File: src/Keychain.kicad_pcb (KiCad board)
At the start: 2 copper layers, 50 x 75 mm, 21 parts, among them M1 Motor_DC, Q1 NPN, SW1 SW_Push

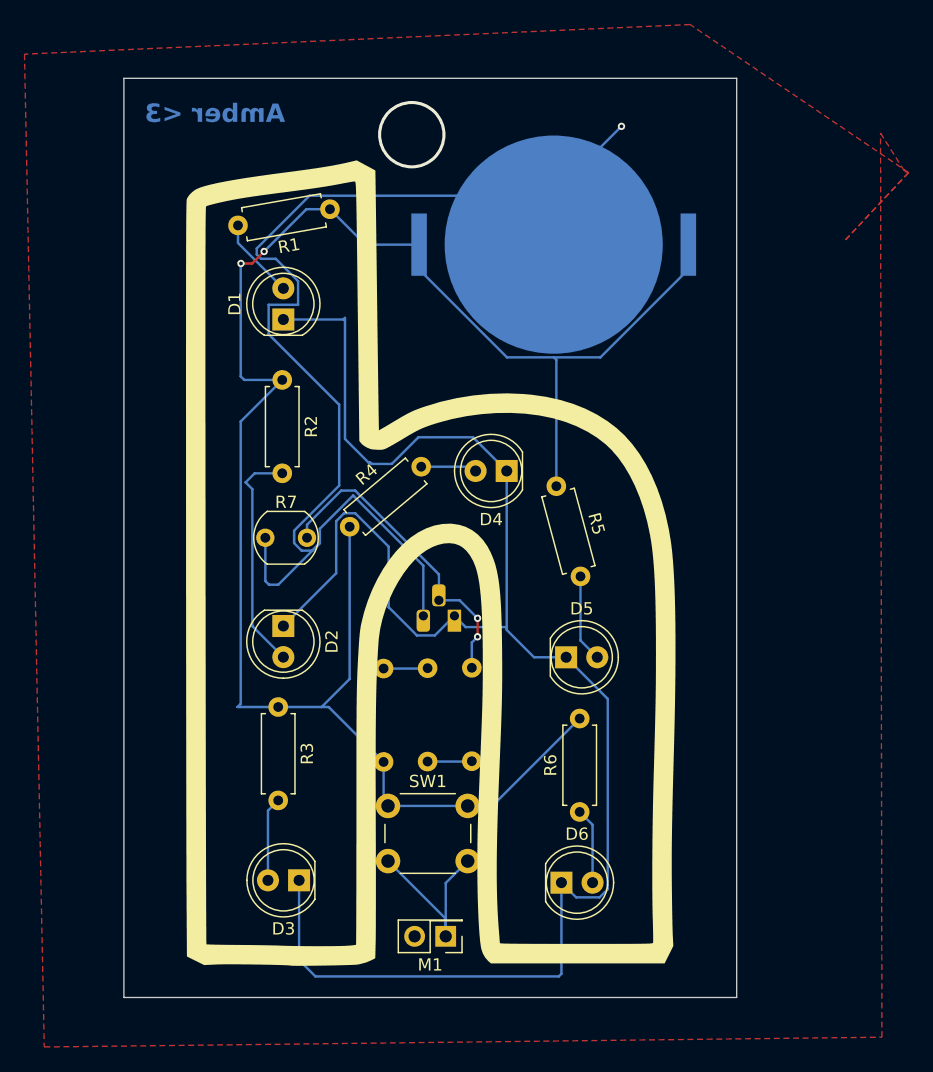
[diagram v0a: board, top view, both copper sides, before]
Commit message: rounded corners!
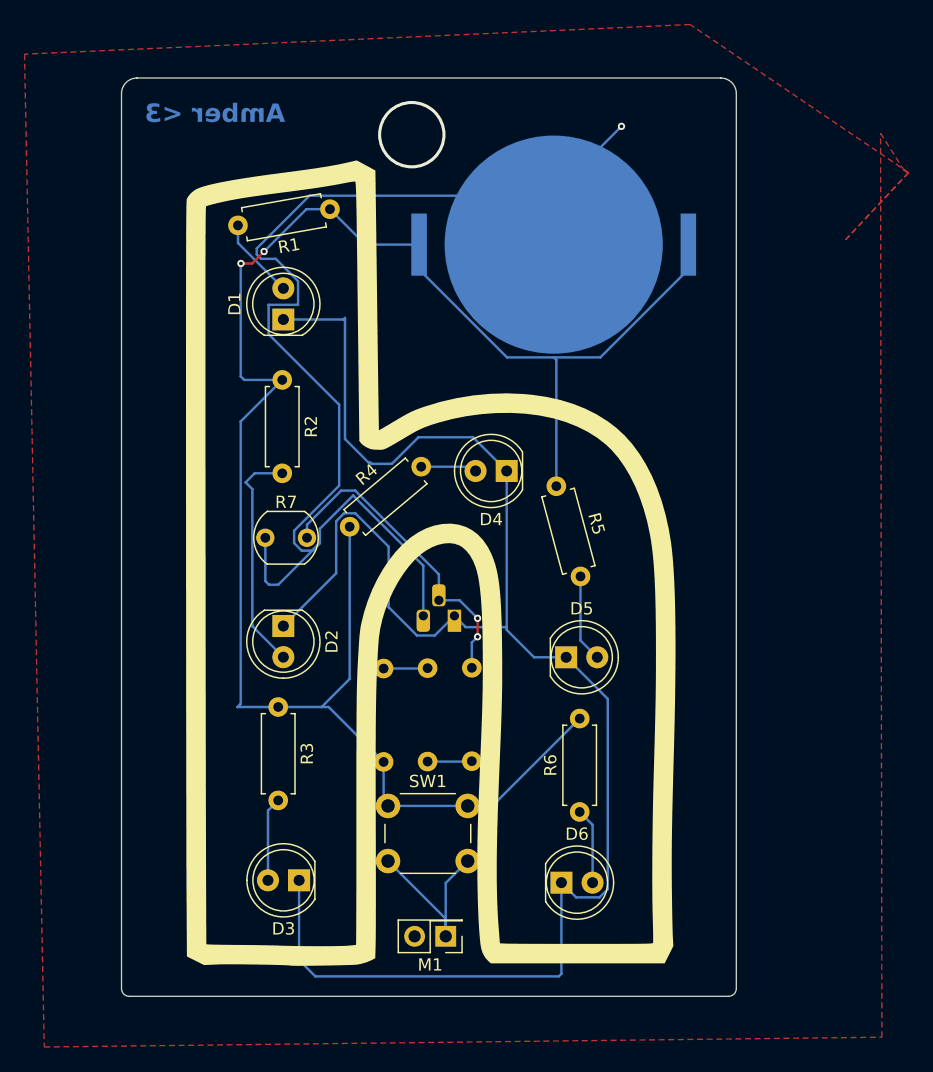
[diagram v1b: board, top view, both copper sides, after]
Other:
- board size 50 x 75 mm -> 50.2 x 74.9 mm
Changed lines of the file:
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@@
 		(tags "tact sw push 6mm")
 		(property "Reference" "SW1"
-			(at 3.25 -2 360)
+			(at 3.25 -2 0)
 			(layer "F.SilkS")
 			(effects
@@
 		)
 		(property "Value" "SW_Push"
-			(at 3.75 6.7 360)
+			(at 3.75 6.7 0)
 			(layer "F.Fab")
 			(effects
@@
 		)
 		(fp_text user "${REFERENCE}"
-			(at 3.25 2.25 360)
+			(at 3.25 2.25 0)
 			(layer "F.Fab")
 			(effects
@@
 		)
 		(fp_text user "${REFERENCE}"
-			(at 8.32 -4.371924 10)
+			(at 8.32 -4.371923 10)
 			(layer "F.Fab")
 			(effects
@@
 		(tags "Through hole pin header THT 2x01 2.54mm double row")
 		(property "Reference" "M1"
-			(at 1.27 -2.33 360)
+			(at 1.27 -2.33 0)
 			(layer "F.SilkS")
 			(effects
@@
 		)
 		(property "Value" "Motor_DC"
-			(at 1.27 2.33 360)
+			(at 1.27 2.33 0)
 			(layer "F.Fab")
 			(effects
@@
 		(tags "Resistor LDR5.1x3.4mm")
 		(property "Reference" "R7"
-			(at 1.7 -2.9 360)
+			(at 1.7 -2.9 0)
 			(layer "F.SilkS")
 			(effects
@@
 		)
 		(property "Value" "R_Photo"
-			(at 1.5 3 360)
+			(at 1.5 3 0)
 			(layer "F.Fab")
 			(effects
@@
 		)
 		(fp_text user "${REFERENCE}"
-			(at 1.7 -2.9 360)
+			(at 1.7 -2.9 0)
 			(layer "F.Fab")
 			(effects
@@
 		(tags "LED")
 		(property "Reference" "D4"
-			(at 1.27 -3.96 360)
+			(at 1.27 -3.96 0)
 			(layer "F.SilkS")
 			(effects
@@
 		)
 		(property "Value" "LED"
-			(at 1.27 3.96 360)
+			(at 1.27 3.96 0)
 			(layer "F.Fab")
 			(effects
@@
 		)
 		(property "Footprint" "LED_THT:LED_D5.0mm"
-			(at 0 0 360)
+			(at 0 0 0)
 			(layer "F.Fab")
 			(hide yes)
@@
 		)
 		(property "Datasheet" ""
-			(at 0 0 360)
+			(at 0 0 0)
 			(layer "F.Fab")
 			(hide yes)
@@
 		)
 		(property "Description" "Light emitting diode"
-			(at 0 0 360)
+			(at 0 0 0)
 			(layer "F.Fab")
 			(hide yes)
@@
 		)
 		(fp_text user "${REFERENCE}"
-			(at 1.27 0 360)
+			(at 1.27 0 0)
 			(layer "F.Fab")
 			(effects
@@
 		(tags "LED")
 		(property "Reference" "D3"
-			(at 1.27 -3.96 360)
+			(at 1.27 -3.96 0)
 			(layer "F.SilkS")
 			(effects
@@
 		)
 		(property "Value" "LED"
-			(at 1.27 3.96 360)
+			(at 1.27 3.96 0)
 			(layer "F.Fab")
 			(effects
@@
 		)
 		(property "Footprint" "LED_THT:LED_D5.0mm"
-			(at 0 0 360)
+			(at 0 0 0)
 			(layer "F.Fab")
 			(hide yes)
@@
 		)
 		(property "Datasheet" ""
-			(at 0 0 360)
+			(at 0 0 0)
 			(layer "F.Fab")
 			(hide yes)
@@
 		)
 		(property "Description" "Light emitting diode"
-			(at 0 0 360)
+			(at 0 0 0)
 			(layer "F.Fab")
 			(hide yes)
@@
 		)
 		(fp_text user "${REFERENCE}"
-			(at 1.27 0 360)
+			(at 1.27 0 0)
 			(layer "F.Fab")
 			(effects
@@
 		)
 		(fp_line
-			(start -1.05 1.5)
+			(start -1.050001 1.5)
 			(end 8.670001 1.499999)
 			(stroke
@@
 		(fp_line
 			(start -1.049999 -1.499999)
-			(end -1.05 1.5)
+			(end -1.050001 1.5)
 			(stroke
 				(width 0.05)
@@
 		)
 		(fp_line
-			(start 0.660002 1.249999)
+			(start 0.660003 1.249999)
 			(end 6.960001 1.250001)
 			(stroke
@@
 		(fp_line
 			(start 0.660001 -1.25)
-			(end 0.660002 1.249999)
+			(end 0.660003 1.249999)
 			(stroke
 				(width 0.1)
@@
 		(tags "to-92 sc-43 sc-43a sot54 PA33 transistor")
 		(property "Reference" "Q1"
-			(at 1.27 3.8 360)
+			(at 1.27 3.8 0)
 			(layer "B.SilkS")
 			(effects
@@
 		)
 		(property "Value" "NPN"
-			(at 1.27 -2.79 360)
+			(at 1.27 -2.79 0)
 			(layer "B.Fab")
 			(effects
@@
 		)
 		(fp_text user "${REFERENCE}"
-			(at 1.27 0 360)
+			(at 1.27 0 0)
 			(layer "B.Fab")
 			(effects
@@
 		)
 	)
-	(gr_rect
-		(start 26.23 19.71)
-		(end 76.23 94.71)
+	(gr_line
+		(start 26.035 93.98)
+		(end 26.035 20.955)
+		(stroke
+			(width 0.05)
+			(type default)
+		)
+		(layer "Edge.Cuts")
+	)
+	(gr_arc
+		(start 26.035 20.955)
+		(mid 26.406974 20.056974)
+		(end 27.305 19.685)
+		(stroke
+			(width 0.05)
+			(type default)
+		)
+		(layer "Edge.Cuts")
+	)
+	(gr_line
+		(start 75.565 94.615)
+		(end 26.67 94.615)
+		(stroke
+			(width 0.05)
+			(type default)
+		)
+		(layer "Edge.Cuts")
+	)
+	(gr_arc
+		(start 26.67 94.615)
+		(mid 26.220987 94.429013)
+		(end 26.035 93.98)
+		(stroke
+			(width 0.05)
+			(type default)
+		)
+		(layer "Edge.Cuts")
+	)
+	(gr_arc
+		(start 76.2 93.98)
+		(mid 76.014013 94.429013)
+		(end 75.565 94.615)
+		(stroke
+			(width 0.05)
+			(type default)
+		)
+		(layer "Edge.Cuts")
+	)
+	(gr_line
+		(start 27.305 19.685)
+		(end 74.93 19.685)
+		(stroke
+			(width 0.05)
+			(type default)
+		)
+		(layer "Edge.Cuts")
+	)
+	(gr_arc
+		(start 74.93 19.685)
+		(mid 75.828026 20.056974)
+		(end 76.2 20.955)
+		(stroke
+			(width 0.05)
+			(type default)
+		)
+		(layer "Edge.Cuts")
+	)
+	(gr_line
+		(start 76.2 20.955)
+		(end 76.2 93.98)
 		(stroke
 			(width 0.05)
 			(type default)
 		)
-		(fill none)
 		(layer "Edge.Cuts")
 	)
